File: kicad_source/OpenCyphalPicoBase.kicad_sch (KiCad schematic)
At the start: 49 parts, among them CN1 RASPBERRYPI_PICO, CN11 CONN_02X03, CN12 Conn_01x03, CN2 SM04B-SRSS-TB, CN3 SM04B-SRSS-TB, CN6 691322310002, CN7 CONN_02X03, CN8 Conn_02x08_Odd_Even, SW1 SPST, U3 24LC64

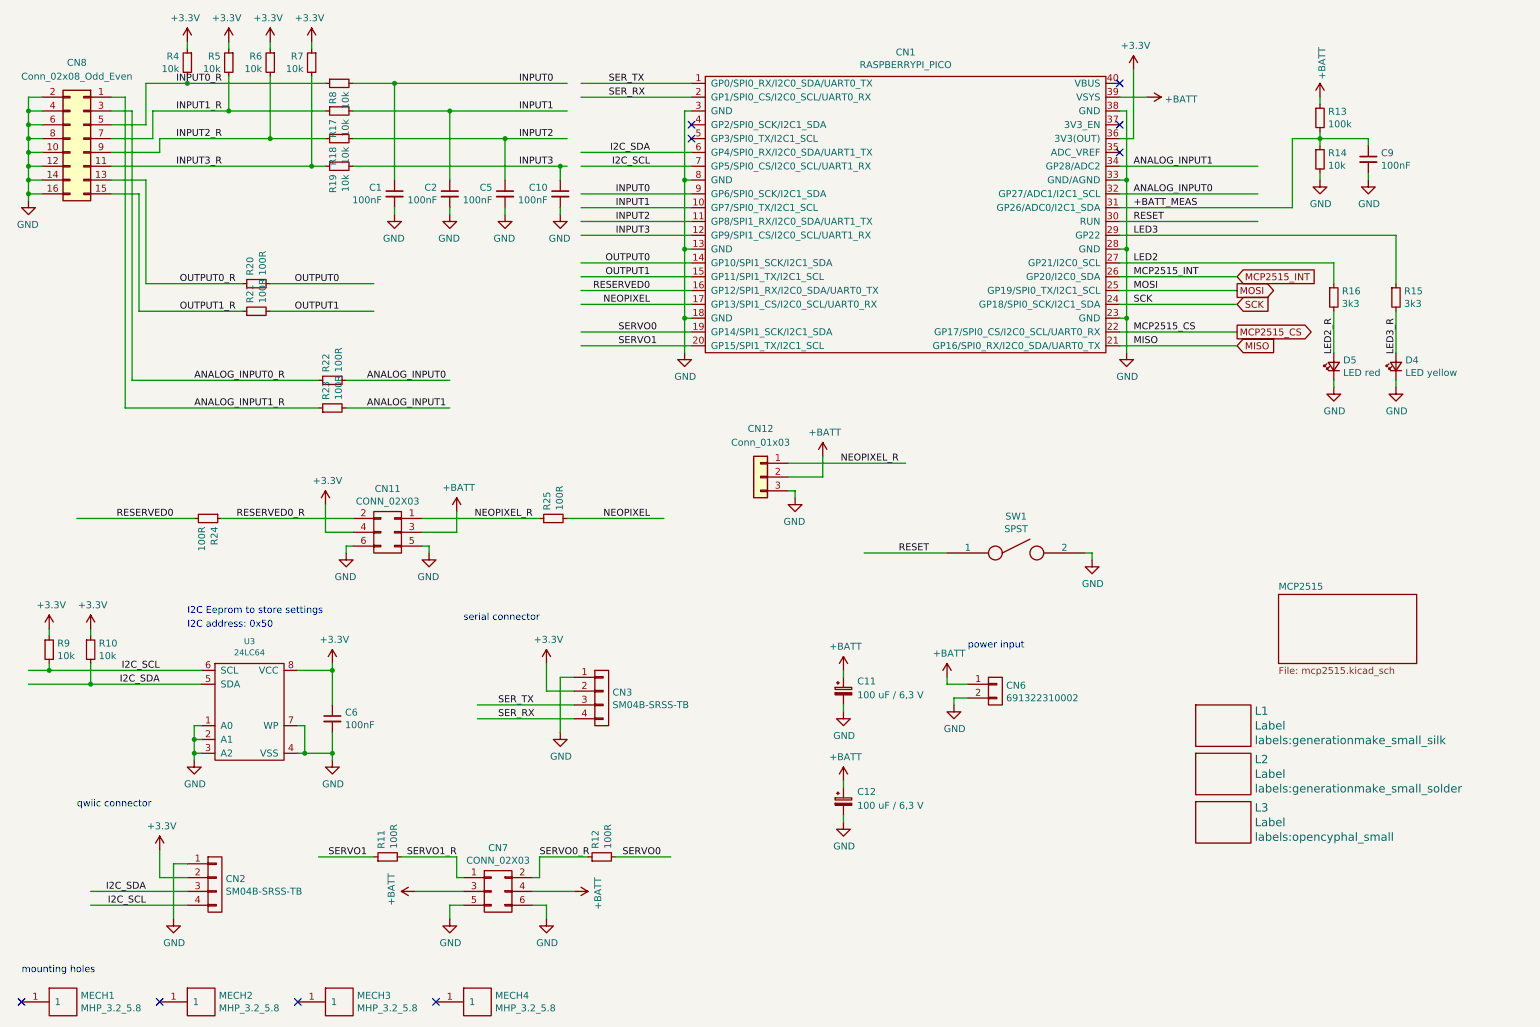
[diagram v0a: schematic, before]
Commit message: clearified some part numbers
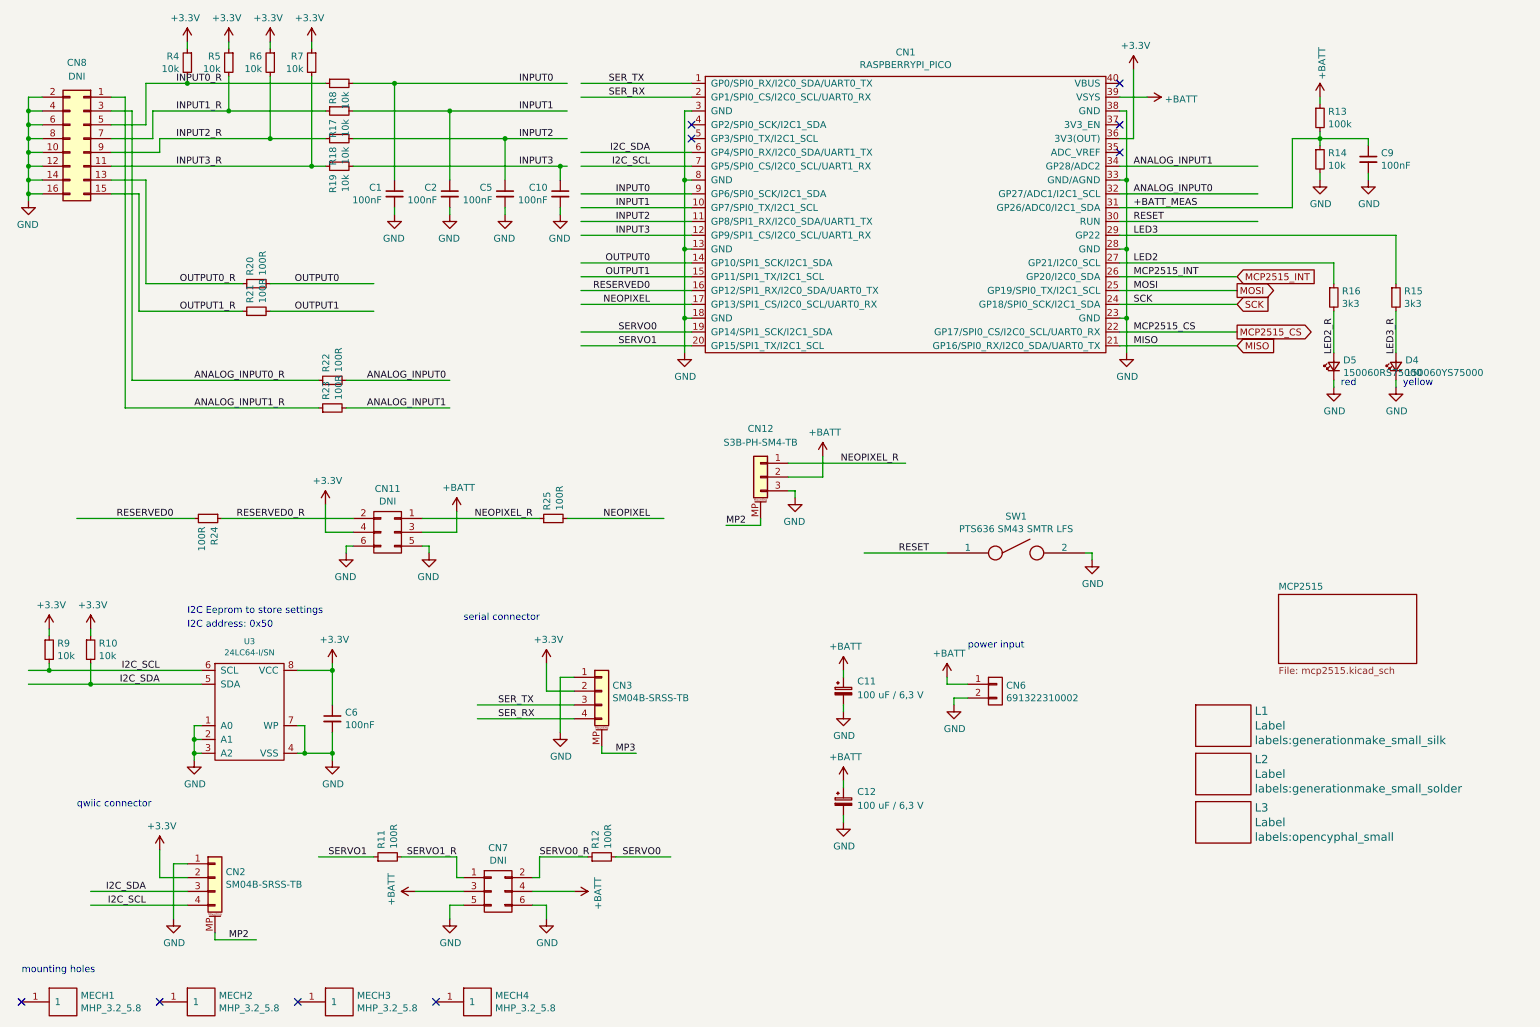
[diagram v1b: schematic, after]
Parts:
- CN1, CN6, L1, L2, L3, MECH1, MECH2, MECH3, MECH4: now left out of the parts list
- CN11, CN7: value CONN_02X03 -> DNI; now left out of the parts list
- CN12: value Conn_01x03 -> S3B-PH-SM4-TB; symbol Connector_Generic:Conn_01x03 -> Connector_Generic_MountingPin:Conn_01x03_MountingPin
- CN2, CN3: symbol OpenCyphalPicoBase-rescue:CONN_01X04-mechanical-connectors -> Connector_Generic_MountingPin:Conn_01x04_MountingPin
- CN8: value Conn_02x08_Odd_Even -> DNI; now left out of the parts list
- D4: value LED yellow -> 150060YS75000
- D5: value LED red -> 150060RS75000
- SW1: value SPST -> PTS636 SM43 SMTR LFS
- U3: value 24LC64 -> 24LC64-I/SN
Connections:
- new net MP2: CN12.MP (MountPin), CN2.MP (MountPin)
- new net MP3: CN3.MP (MountPin)
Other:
- note added: "red"
- note added: "yellow"

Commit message: added some JLCPCB part numbers and BOM
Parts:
- C1, C10, C2, C5, C6, C9: LCSC (none) -> C314282
- CN12: LCSC (none) -> C265101
- CN2, CN3: LCSC (none) -> C160404
- R10, R13, R14, R17, R18, R19, R4, R5, R6, R7, R8, R9: LCSC (none) -> C3152123
- R11, R12, R20, R21, R22, R23, R24, R25: LCSC (none) -> C105588
- R15, R16: LCSC (none) -> C108078
- U3: LCSC (none) -> C3007892
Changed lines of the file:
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@@
+      (effects (font (size 1.27 1.27)) hide)
+    )
+    (property "LCSC" "C160404" (id 4) (at 124.46 135.89 0)
       (effects (font (size 1.27 1.27)) hide)
     )
@@
     )
     (property "Datasheet" "" (id 3) (at 22.86 128.27 0))
+    (property "LCSC" "C3152123" (id 4) (at 22.86 128.27 0)
+      (effects (font (size 1.27 1.27)) hide)
+    )
     (pin "1")
     (pin "2")
@@
     )
     (property "Datasheet" "" (id 3) (at 30.48 128.27 0))
+    (property "LCSC" "C3152123" (id 4) (at 30.48 128.27 0)
+      (effects (font (size 1.27 1.27)) hide)
+    )
     (pin "1")
     (pin "2")
@@
       (effects (font (size 1.27 1.27)) hide)
     )
+    (property "LCSC" "C160404" (id 4) (at 53.34 170.18 0)
+      (effects (font (size 1.27 1.27)) hide)
+    )
     (pin "1")
     (pin "2")
@@
     )
     (property "Datasheet" "" (id 3) (at 124.46 166.37 0))
+    (property "LCSC" "C105588" (id 4) (at 124.46 166.37 0)
+      (effects (font (size 1.27 1.27)) hide)
+    )
     (pin "1")
     (pin "2")
@@
     )
     (property "Datasheet" "" (id 3) (at 85.09 166.37 0))
+    (property "LCSC" "C105588" (id 4) (at 85.09 166.37 0)
+      (effects (font (size 1.27 1.27)) hide)
+    )
     (pin "1")
     (pin "2")
@@
     (property "Datasheet" "" (id 3) (at 59.69 139.7 0)
       (effects (font (size 1.0922 1.0922)) hide)
+    )
+    (property "LCSC" "C3007892" (id 4) (at 59.69 139.7 0)
+      (effects (font (size 1.27 1.27)) hide)
     )
     (pin "1")
@@
     )
     (property "Datasheet" "" (id 3) (at 74.93 140.97 0))
+    (property "LCSC" "C314282" (id 4) (at 74.93 140.97 0)
+      (effects (font (size 1.27 1.27)) hide)
+    )
     (pin "1")
     (pin "2")
@@
     )
     (property "Datasheet" "" (id 3) (at 259.08 63.5 0))
+    (property "LCSC" "C108078" (id 4) (at 259.08 63.5 0)
+      (effects (font (size 1.27 1.27)) hide)
+    )
     (pin "1")
     (pin "2")
@@
     )
     (property "Datasheet" "" (id 3) (at 270.51 63.5 0))
+    (property "LCSC" "C108078" (id 4) (at 270.51 63.5 0)
+      (effects (font (size 1.27 1.27)) hide)
+    )
     (pin "1")
     (pin "2")
@@
     )
     (property "Datasheet" "" (id 3) (at 256.54 30.48 0))
+    (property "LCSC" "C3152123" (id 4) (at 256.54 30.48 0)
+      (effects (font (size 1.27 1.27)) hide)
+    )
     (pin "1")
     (pin "2")
@@
     )
     (property "Datasheet" "" (id 3) (at 256.54 38.1 0))
+    (property "LCSC" "C3152123" (id 4) (at 256.54 38.1 0)
+      (effects (font (size 1.27 1.27)) hide)
+    )
     (pin "1")
     (pin "2")
@@
     )
     (property "Datasheet" "" (id 3) (at 265.43 38.1 0))
+    (property "LCSC" "C314282" (id 4) (at 265.43 38.1 0)
+      (effects (font (size 1.27 1.27)) hide)
+    )
     (pin "1")
     (pin "2")
@@
     )
     (property "Datasheet" "" (id 3) (at 48.26 20.32 0))
+    (property "LCSC" "C3152123" (id 4) (at 48.26 20.32 0)
+      (effects (font (size 1.27 1.27)) hide)
+    )
     (pin "1")
     (pin "2")
@@
     )
     (property "Datasheet" "" (id 3) (at 55.88 20.32 0))
+    (property "LCSC" "C3152123" (id 4) (at 55.88 20.32 0)
+      (effects (font (size 1.27 1.27)) hide)
+    )
     (pin "1")
     (pin "2")
@@
     )
     (property "Datasheet" "" (id 3) (at 63.5 20.32 0))
+    (property "LCSC" "C3152123" (id 4) (at 63.5 20.32 0)
+      (effects (font (size 1.27 1.27)) hide)
+    )
     (pin "1")
     (pin "2")
@@
     )
     (property "Datasheet" "" (id 3) (at 71.12 20.32 0))
+    (property "LCSC" "C3152123" (id 4) (at 71.12 20.32 0)
+      (effects (font (size 1.27 1.27)) hide)
+    )
     (pin "1")
     (pin "2")
@@
     )
     (property "Datasheet" "" (id 3) (at 76.2 24.13 0))
+    (property "LCSC" "C3152123" (id 4) (at 76.2 24.13 0)
+      (effects (font (size 1.27 1.27)) hide)
+    )
     (pin "1")
     (pin "2")
@@
     )
     (property "Datasheet" "" (id 3) (at 76.2 29.21 0))
+    (property "LCSC" "C3152123" (id 4) (at 76.2 29.21 0)
+      (effects (font (size 1.27 1.27)) hide)
+    )
     (pin "1")
     (pin "2")
@@
     )
     (property "Datasheet" "" (id 3) (at 76.2 34.29 0))
+    (property "LCSC" "C3152123" (id 4) (at 76.2 34.29 0)
+      (effects (font (size 1.27 1.27)) hide)
+    )
     (pin "1")
     (pin "2")
@@
     )
     (property "Datasheet" "" (id 3) (at 76.2 39.37 0))
+    (property "LCSC" "C3152123" (id 4) (at 76.2 39.37 0)
+      (effects (font (size 1.27 1.27)) hide)
+    )
     (pin "1")
     (pin "2")
@@
     )
     (property "Datasheet" "" (id 3) (at 86.36 44.45 0))
+    (property "LCSC" "C314282" (id 4) (at 86.36 44.45 0)
+      (effects (font (size 1.27 1.27)) hide)
+    )
     (pin "1")
     (pin "2")
@@
     )
     (property "Datasheet" "" (id 3) (at 96.52 44.45 0))
+    (property "LCSC" "C314282" (id 4) (at 96.52 44.45 0)
+      (effects (font (size 1.27 1.27)) hide)
+    )
     (pin "1")
     (pin "2")
@@
     )
     (property "Datasheet" "" (id 3) (at 106.68 44.45 0))
+    (property "LCSC" "C314282" (id 4) (at 106.68 44.45 0)
+      (effects (font (size 1.27 1.27)) hide)
+    )
     (pin "1")
     (pin "2")
@@
     )
     (property "Datasheet" "" (id 3) (at 116.84 44.45 0))
+    (property "LCSC" "C314282" (id 4) (at 116.84 44.45 0)
+      (effects (font (size 1.27 1.27)) hide)
+    )
     (pin "1")
     (pin "2")
@@
     )
     (property "Datasheet" "" (id 3) (at 60.96 60.96 0))
+    (property "LCSC" "C105588" (id 4) (at 60.96 60.96 0)
+      (effects (font (size 1.27 1.27)) hide)
+    )
     (pin "1")
     (pin "2")
@@
     )
     (property "Datasheet" "" (id 3) (at 60.96 66.04 0))
+    (property "LCSC" "C105588" (id 4) (at 60.96 66.04 0)
+      (effects (font (size 1.27 1.27)) hide)
+    )
     (pin "1")
     (pin "2")
@@
     )
     (property "Datasheet" "" (id 3) (at 74.93 78.74 0))
+    (property "LCSC" "C105588" (id 4) (at 74.93 78.74 0)
+      (effects (font (size 1.27 1.27)) hide)
+    )
     (pin "1")
     (pin "2")
@@
     )
     (property "Datasheet" "" (id 3) (at 74.93 83.82 0))
+    (property "LCSC" "C105588" (id 4) (at 74.93 83.82 0)
+      (effects (font (size 1.27 1.27)) hide)
+    )
     (pin "1")
     (pin "2")
@@
     )
     (property "Datasheet" "" (id 3) (at 52.07 104.14 0))
+    (property "LCSC" "C105588" (id 4) (at 52.07 104.14 0)
+      (effects (font (size 1.27 1.27)) hide)
+    )
     (pin "1")
     (pin "2")
@@
     )
     (property "Datasheet" "" (id 3) (at 115.57 104.14 0))
+    (property "LCSC" "C105588" (id 4) (at 115.57 104.14 0)
+      (effects (font (size 1.27 1.27)) hide)
+    )
     (pin "1")
     (pin "2")
@@
       (effects (font (size 1.27 1.27)) hide)
     )
+    (property "LCSC" "C265101" (id 4) (at 153.67 96.52 0)
+      (effects (font (size 1.27 1.27)) hide)
+    )
     (pin "1")
     (pin "2")
@@
     )
     (path "/00000000-0000-0000-0000-00005ed92f9c/00000000-0000-0000-0000-00005ed9419d"
-      (reference "U8") (unit 1) (value "MCP2515-I/SO") (footprint "Package_SO:SOIC-18W_7.5x11.6mm_P1.27mm")
+      (reference "U8") (unit 1) (value "MCP2515T-I/SO") (footprint "Package_SO:SOIC-18W_7.5x11.6mm_P1.27mm")
     )
     (path "/00000000-0000-0000-0000-00005ed92f9c/00000000-0000-0000-0000-00005edabfb3"

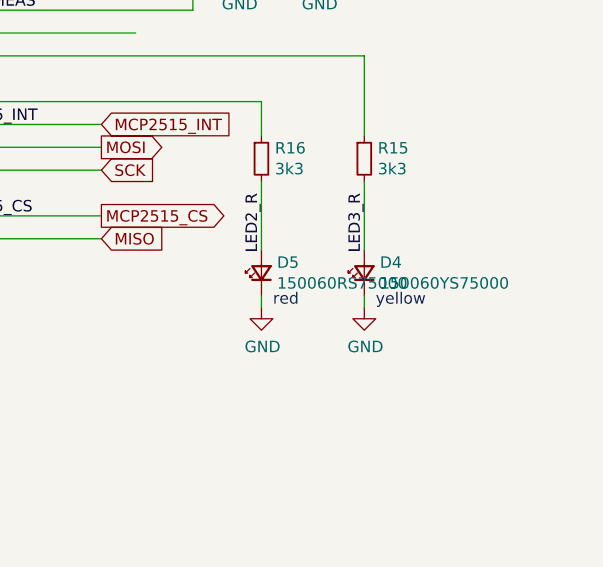
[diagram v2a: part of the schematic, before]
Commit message: added missing JLCPCB part numbers
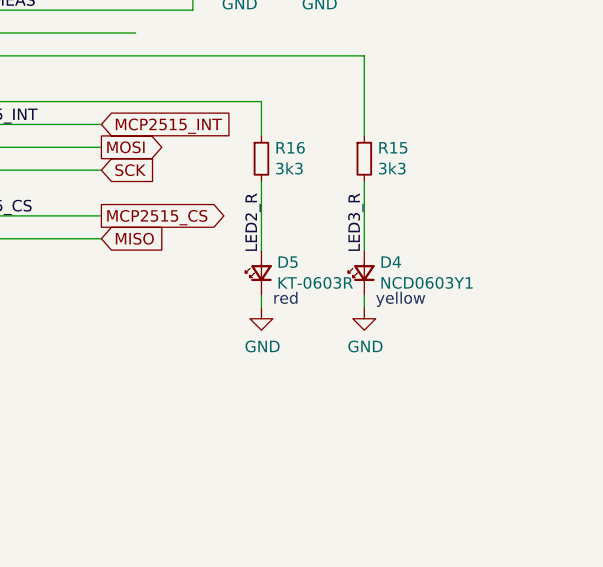
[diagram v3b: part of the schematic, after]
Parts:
- C11, C12: LCSC (none) -> C3001204
- D4: value 150060YS75000 -> NCD0603Y1; LCSC (none) -> C84268
- D5: value 150060RS75000 -> KT-0603R; LCSC (none) -> C2286
- R13: LCSC C3152123 -> C25803
- SW1: LCSC (none) -> C2800965
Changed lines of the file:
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@@
       (effects (font (size 1.27 1.27)) (justify right))
     )
-    (property "Value" "150060RS75000" (id 1) (at 260.8072 77.343 90)
+    (property "Value" "KT-0603R" (id 1) (at 260.8072 77.343 90)
       (effects (font (size 1.27 1.27)) (justify right))
     )
@@
     )
     (property "Datasheet" "" (id 3) (at 259.08 76.2 90))
+    (property "LCSC" "C2286" (id 4) (at 259.08 76.2 90)
+      (effects (font (size 1.27 1.27)) hide)
+    )
     (pin "1")
     (pin "2")
@@
       (effects (font (size 1.27 1.27)) (justify right))
     )
-    (property "Value" "150060YS75000" (id 1) (at 272.2372 77.343 90)
+    (property "Value" "NCD0603Y1" (id 1) (at 272.2372 77.343 90)
       (effects (font (size 1.27 1.27)) (justify right))
     )
@@
     )
     (property "Datasheet" "" (id 3) (at 270.51 76.2 90))
+    (property "LCSC" "C84268" (id 4) (at 270.51 76.2 90)
+      (effects (font (size 1.27 1.27)) hide)
+    )
     (pin "1")
     (pin "2")
@@
     )
     (property "Datasheet" "" (id 3) (at 256.54 30.48 0))
-    (property "LCSC" "C3152123" (id 4) (at 256.54 30.48 0)
+    (property "LCSC" "C25803" (id 4) (at 256.54 30.48 0)
       (effects (font (size 1.27 1.27)) hide)
     )
@@
     )
     (property "Datasheet" "" (id 3) (at 200.66 110.49 0))
+    (property "LCSC" "C2800965" (id 4) (at 200.66 110.49 0)
+      (effects (font (size 1.27 1.27)) hide)
+    )
     (pin "1")
     (pin "2")
@@
     )
     (property "Datasheet" "~" (id 3) (at 168.91 156.21 0)
+      (effects (font (size 1.27 1.27)) hide)
+    )
+    (property "LCSC" "C3001204" (id 4) (at 168.91 156.21 0)
       (effects (font (size 1.27 1.27)) hide)
     )
@@
       (effects (font (size 1.27 1.27)) hide)
     )
+    (property "LCSC" "C3001204" (id 4) (at 168.91 135.89 0)
+      (effects (font (size 1.27 1.27)) hide)
+    )
     (pin "1")
     (pin "2")
@@
     )
     (path "/00000000-0000-0000-0000-000062572e1d"
-      (reference "D4") (unit 1) (value "150060YS75000") (footprint "LED_SMD:LED_0603_1608Metric")
+      (reference "D4") (unit 1) (value "NCD0603Y1") (footprint "LED_SMD:LED_0603_1608Metric")
     )
     (path "/00000000-0000-0000-0000-00006256c144"
-      (reference "D5") (unit 1) (value "150060RS75000") (footprint "LED_SMD:LED_0603_1608Metric")
+      (reference "D5") (unit 1) (value "KT-0603R") (footprint "LED_SMD:LED_0603_1608Metric")
     )
     (path "/00000000-0000-0000-0000-00005ed92f9c/b9849e65-1d07-4975-a6c6-58bb911480e0"
-      (reference "F1") (unit 1) (value "nanoSMDC050F") (footprint "Fuse:Fuse_1206_3216Metric")
+      (reference "F1") (unit 1) (value "nSMD050-33V") (footprint "Fuse:Fuse_1206_3216Metric")
     )
     (path "/00000000-0000-0000-0000-0000625bb6fe"
@@
     )
     (path "/00000000-0000-0000-0000-00005ed92f9c/00000000-0000-0000-0000-00005ed95d76"
-      (reference "Y1") (unit 1) (value "RH100-16.000-16-3030-EXT-TR") (footprint "crystals:Crystal_SMD_3.2x2.5mm_4Pad")
-    )
-  )
+      (reference "Y1") (unit 1) (value "X322516MLB4SI") (footprint "crystals:Crystal_SMD_3.2x2.5mm_4Pad")
+    )
+  )
